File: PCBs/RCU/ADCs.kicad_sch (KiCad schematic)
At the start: 12 parts, among them U600 ADC121C027CIMK/NOPB, U601 OPA365xxD, U602 ADC121C027CIMK/NOPB, U603 OPA365xxD

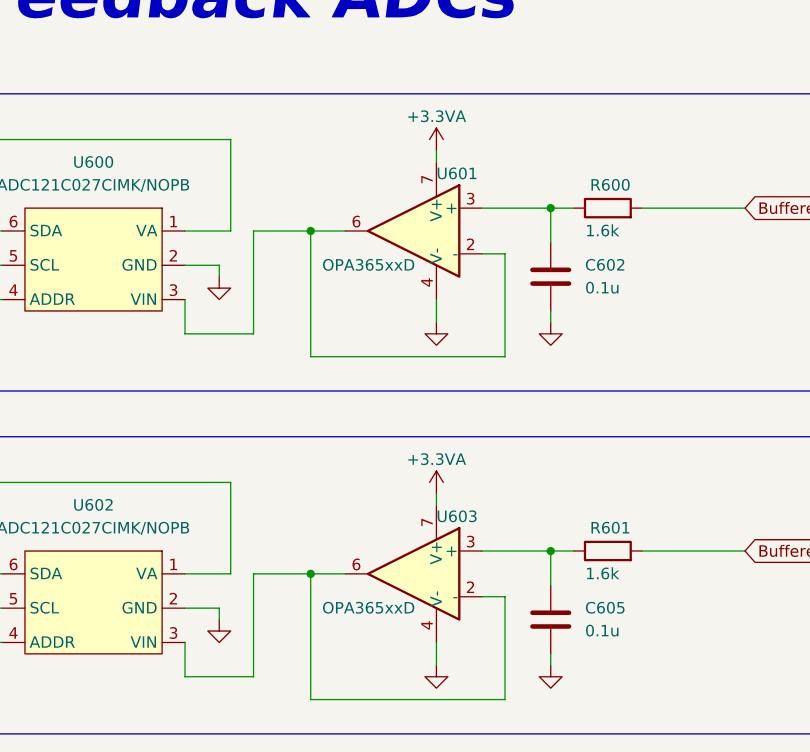
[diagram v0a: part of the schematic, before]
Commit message: Replaced OPA365 op amps with OPA320 op amps
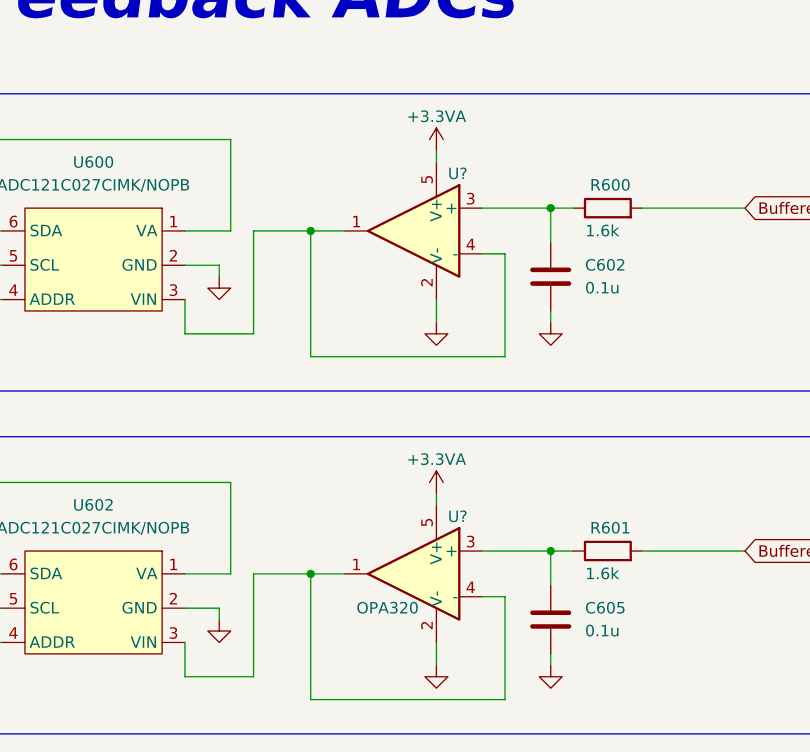
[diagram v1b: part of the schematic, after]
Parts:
- removed U601, U603: OPA365xxD, Package_SO:SOIC-8_3.9x4.9mm_P1.27mm, symbol Amplifier_Operational:OPA365xxD
- added U?: (no value), symbol Amplifier_Operational:OPA330xxDBV
- added U?: OPA320, Package_TO_SOT_SMD:SOT-23-5, symbol Amplifier_Operational:OPA330xxDBV
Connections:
- net +3.3VA: now also U?.5 (V+), U?.5 (V+)
- net GND: now also U?.2 (V-), U?.2 (V-)
- net at C602.2, R600.1: now also U?.3 (+)
- net at C605.2, R601.1: now also U?.3 (+)
- net at U602.3 (VIN): now also U?.1, U?.4 (-)
- net at U600.3 (VIN): now also U?.1, U?.4 (-)

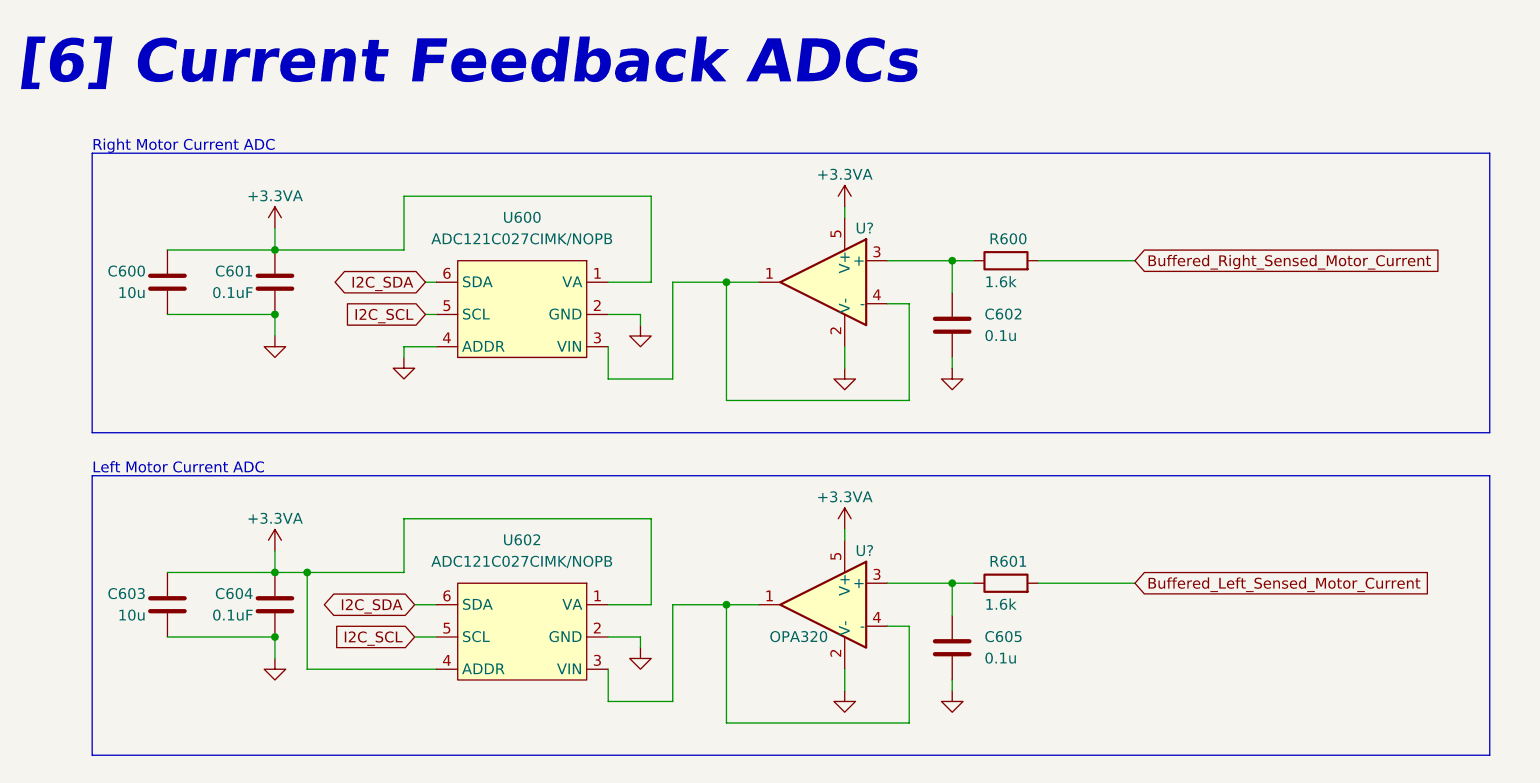
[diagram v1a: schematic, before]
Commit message: Add bypass caps to omp amps in sensors module
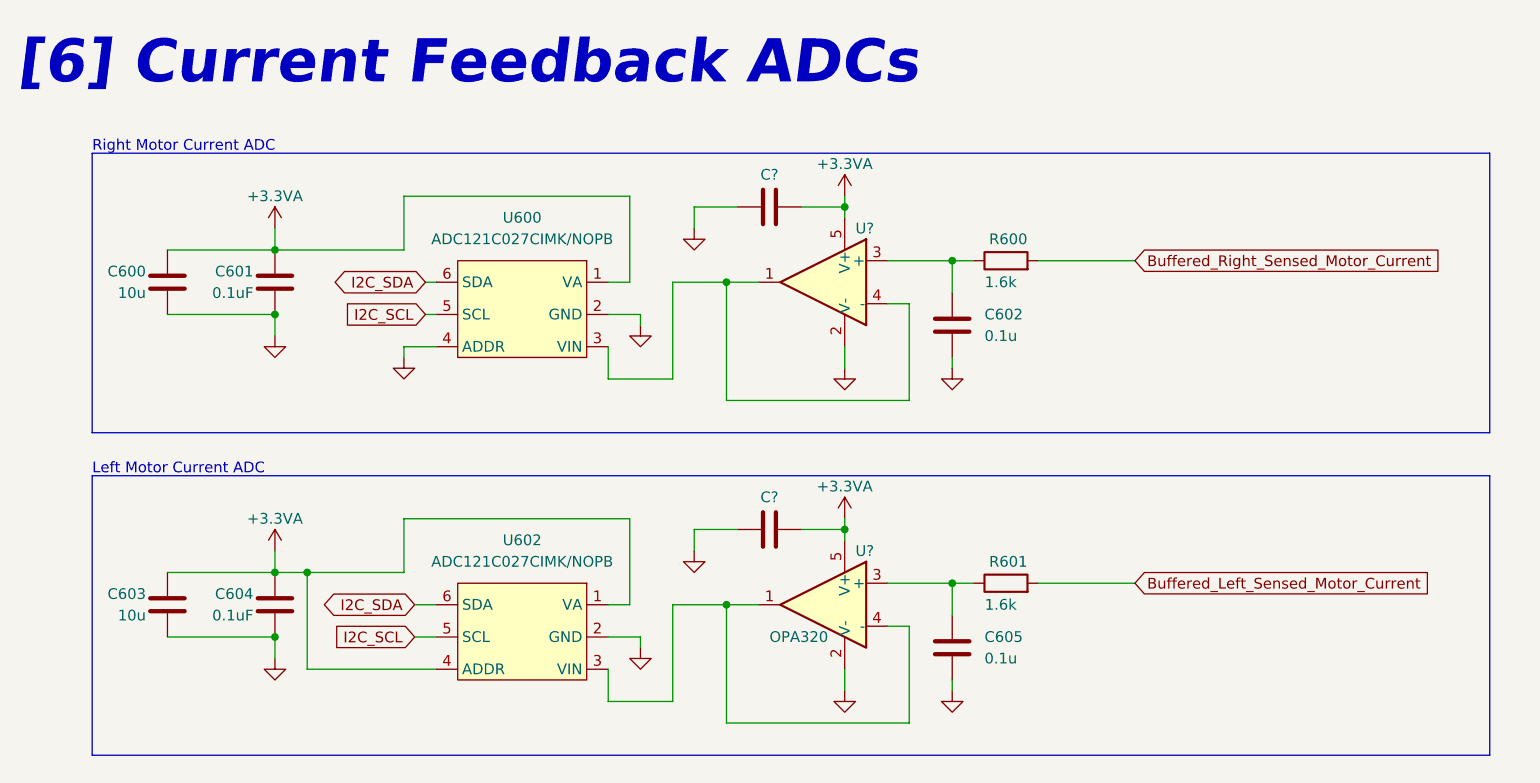
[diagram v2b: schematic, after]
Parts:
- added C? (x2): (no value), symbol Device:C
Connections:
- net +3.3VA: now also C?.2, C?.2
- net GND: now also C?.1, C?.1

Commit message: Updated ADC schematic to match application note in ADC and op-amp data sheets
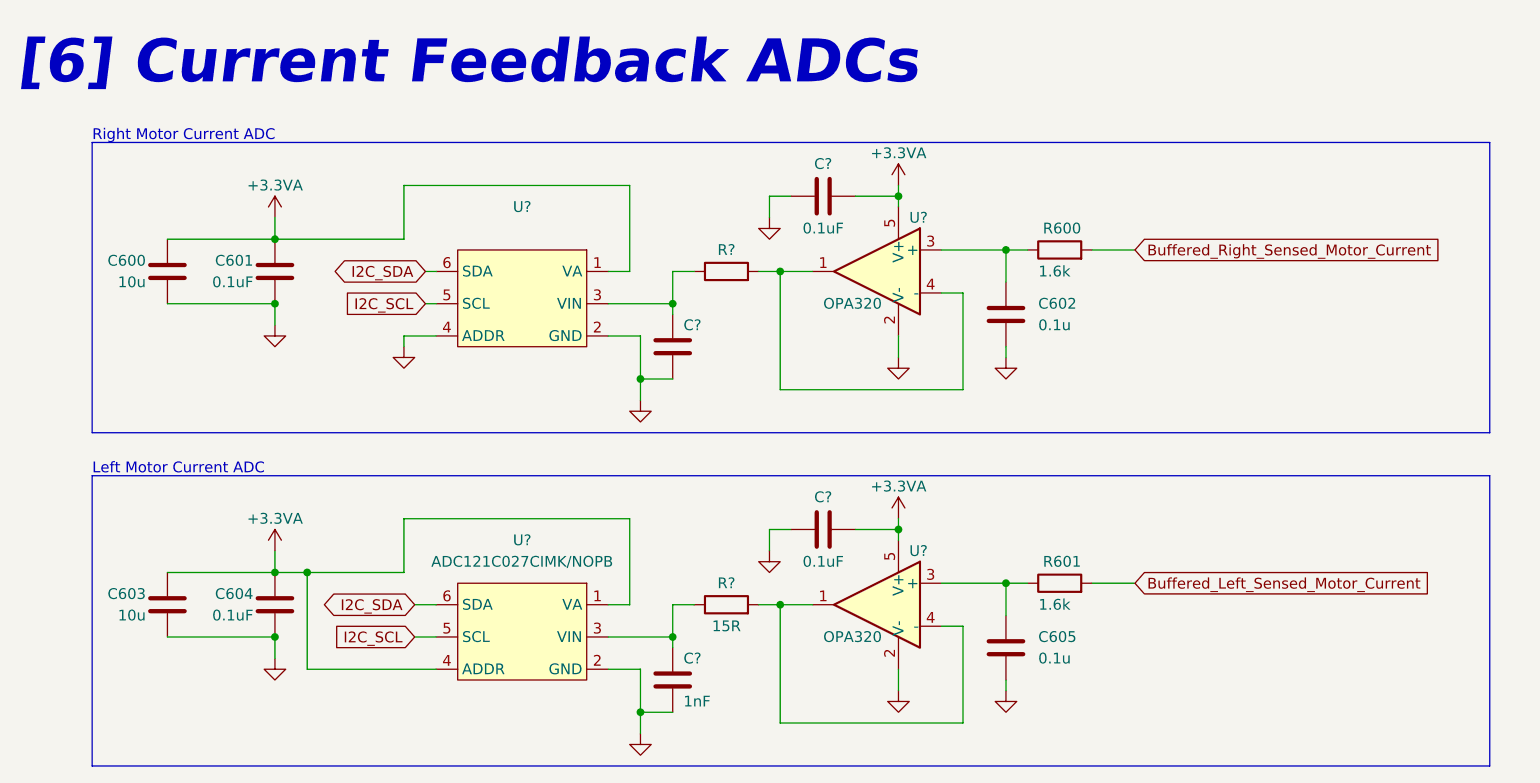
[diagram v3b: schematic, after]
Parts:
- removed U600, U602: ADC121C027CIMK/NOPB, symbol Ghanis_Symbols_KiCad6:ADC121C027CIMK/NOPB
- added C?: 1nF, symbol Device:C
- added C?: (no value), symbol Device:C
- added R?: (no value), symbol Device:R
- added R?: 15R, symbol Device:R
- added U?: (no value), symbol Ghanis_Symbols_KiCad6:ADC121C027CIMK/NOPB
- added U?: ADC121C027CIMK/NOPB, symbol Ghanis_Symbols_KiCad6:ADC121C027CIMK/NOPB
- C? (x2): value (none) -> 0.1uF
- U?: value (none) -> OPA320; footprint (none) -> Package_TO_SOT_SMD:SOT-23-5
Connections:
- net +3.3VA: now also U?.1 (VA), U?.1 (VA), U?.4 (ADDR)
- net GND: now also C?.2, C?.2, U?.2 (GND), U?.2 (GND), U?.4 (ADDR)
- net I2C_SCL: now also U?.5 (SCL), U?.5 (SCL)
- net I2C_SDA: now also U?.6 (SDA), U?.6 (SDA)
- net at U?.1, U?.4 (-): now also R?.2 (x2)
- new net: C?.1, R?.1, U?.3 (VIN) (x2)
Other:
- moved on the sheet: C600, C601, C602, C605, C?, R600, R601, U?

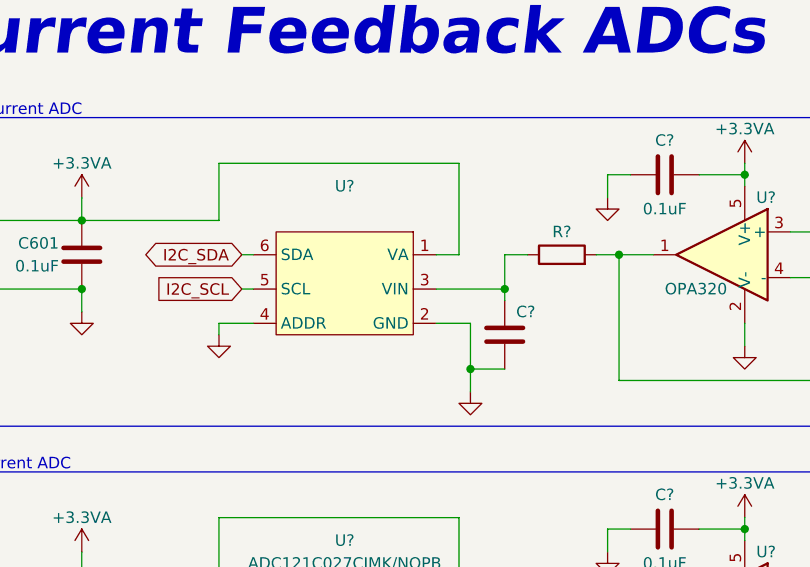
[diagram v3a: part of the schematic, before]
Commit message: Changed values for R100 and C108
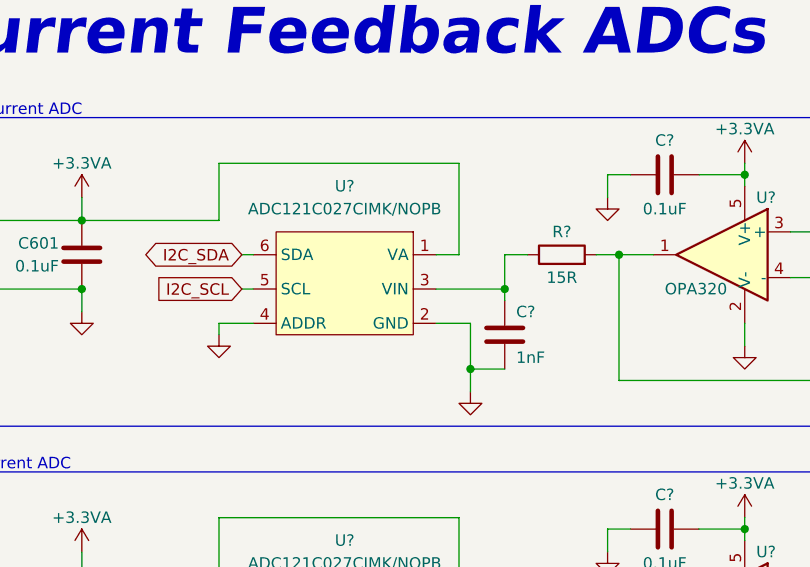
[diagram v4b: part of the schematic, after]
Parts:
- C?: value (none) -> 1nF
- R?: value (none) -> 15R
- U?: value (none) -> ADC121C027CIMK/NOPB
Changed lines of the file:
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@@
     (in_bom yes) (on_board yes)
     (property "Reference" "R?" (id 0) (at 99.06 41.91 90))
-    (property "Value" "" (id 1) (at 99.06 46.99 90))
+    (property "Value" "15R" (id 1) (at 99.06 46.99 90))
     (property "Footprint" "" (id 2) (at 99.06 46.228 90)
       (effects (font (size 1.27 1.27)) hide)
@@
       (effects (font (size 1.27 1.27)) (justify left))
     )
-    (property "Value" "" (id 1) (at 93.98 55.88 0)
+    (property "Value" "1nF" (id 1) (at 93.98 55.88 0)
       (effects (font (size 1.27 1.27)) (justify left))
     )
@@
     (in_bom yes) (on_board yes) (fields_autoplaced)
     (property "Reference" "U?" (id 0) (at 74.93 36.83 0))
-    (property "Value" "" (id 1) (at 74.93 39.37 0))
+    (property "Value" "ADC121C027CIMK/NOPB" (id 1) (at 74.93 39.37 0))
     (property "Footprint" "" (id 2) (at 85.09 38.1 0)
       (effects (font (size 1.27 1.27)) hide)
